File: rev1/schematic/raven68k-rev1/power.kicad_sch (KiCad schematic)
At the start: 36 parts, among them IC1 L5970D013TR, IC2 L5970D013TR, J3 Jack-DC, SW2 POWER_SW

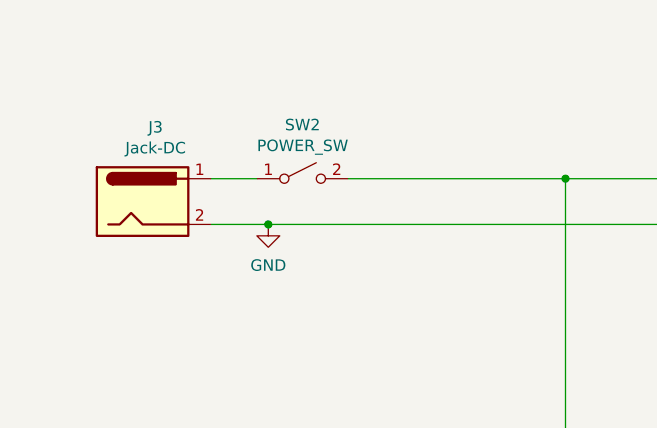
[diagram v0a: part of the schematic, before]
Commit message: board layout complete, needs verification
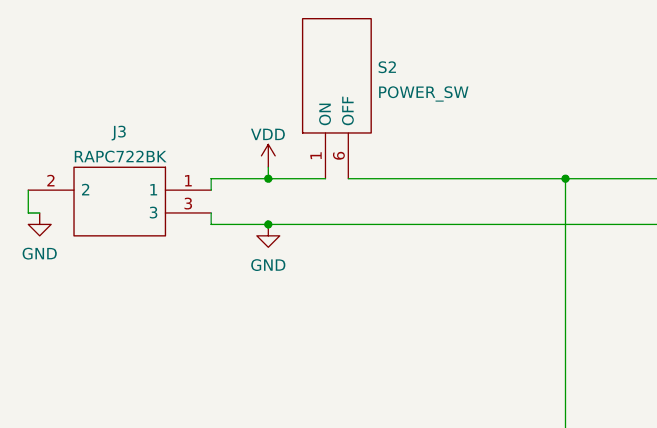
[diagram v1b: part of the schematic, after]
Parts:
- removed J3: Jack-DC, raven68k-rev1:RAPC722BK, symbol Connector:Jack-DC
- removed SW2: POWER_SW, raven68k-rev1:10TC605, symbol Switch:SW_SPST
- added J3: RAPC722BK, raven68k-rev1:RAPC722BK, symbol custom:RAPC722BK
- added S2: POWER_SW, raven68k-rev1:GPTS203212B, symbol custom:GPTS203212B
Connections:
- net GND: now also J3.2, J3.3
- net at C12.2, C13.2, C14.2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: now also S2.6 (OFF)
- new net VDD: J3.1, S2.1 (ON)
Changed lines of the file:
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@@
 (kicad_sch (version 20211123) (generator eeschema)
   (paper "A4")
+  (junction (at 73.66 57.15) (diameter 0) (color 0 0 0 0)
+  )
   (junction (at 231.14 53.34) (diameter 0) (color 0 0 0 0)
   )
@@
   (junction (at 254 149.86) (diameter 0) (color 0 0 0 0)
   )
+  (junction (at 40.64 57.15) (diameter 0) (color 0 0 0 0)
+  )
   (junction (at 231.14 115.57) (diameter 0) (color 0 0 0 0)
   )
@@
   )
   (junction (at 124.46 64.77) (diameter 0) (color 0 0 0 0)
-  )
-  (junction (at 73.66 57.15) (diameter 0) (color 0 0 0 0)
   )
   (junction (at 242.57 87.63) (diameter 0) (color 0 0 0 0)
@@
     (stroke (width 0) (type default) (color 0 0 0 0))
   )
+  (wire (pts (xy 34.29 57.15) (xy 34.29 58.42))
+    (stroke (width 0) (type default) (color 0 0 0 0))
+  )
   (wire (pts (xy 134.62 130.81) (xy 134.62 127))
     (stroke (width 0) (type default) (color 0 0 0 0))
@@
     (stroke (width 0) (type default) (color 0 0 0 0))
   )
+  (wire (pts (xy 40.64 57.15) (xy 46.99 57.15))
+    (stroke (width 0) (type default) (color 0 0 0 0))
+  )
   (wire (pts (xy 201.93 81.28) (xy 201.93 87.63))
     (stroke (width 0) (type default) (color 0 0 0 0))
@@
     (stroke (width 0) (type default) (color 0 0 0 0))
   )
+  (wire (pts (xy 40.64 55.88) (xy 40.64 57.15))
+    (stroke (width 0) (type default) (color 0 0 0 0))
+  )
   (wire (pts (xy 219.71 71.12) (xy 219.71 63.5))
     (stroke (width 0) (type default) (color 0 0 0 0))
@@
     (stroke (width 0) (type default) (color 0 0 0 0))
   )
+  (wire (pts (xy 13.97 58.42) (xy 13.97 60.96))
+    (stroke (width 0) (type default) (color 0 0 0 0))
+  )
   (wire (pts (xy 134.62 87.63) (xy 152.4 87.63))
     (stroke (width 0) (type default) (color 0 0 0 0))
@@
     (stroke (width 0) (type default) (color 0 0 0 0))
   )
+  (wire (pts (xy 49.53 57.15) (xy 73.66 57.15))
+    (stroke (width 0) (type default) (color 0 0 0 0))
+  )
   (wire (pts (xy 266.7 59.69) (xy 266.7 53.34))
     (stroke (width 0) (type default) (color 0 0 0 0))
@@
     (stroke (width 0) (type default) (color 0 0 0 0))
   )
+  (wire (pts (xy 34.29 60.96) (xy 34.29 62.23))
+    (stroke (width 0) (type default) (color 0 0 0 0))
+  )
   (wire (pts (xy 86.36 62.23) (xy 86.36 87.63))
     (stroke (width 0) (type default) (color 0 0 0 0))
   )
-  (wire (pts (xy 34.29 57.15) (xy 39.37 57.15))
-    (stroke (width 0) (type default) (color 0 0 0 0))
-  )
   (wire (pts (xy 73.66 57.15) (xy 104.14 57.15))
     (stroke (width 0) (type default) (color 0 0 0 0))
@@
     (stroke (width 0) (type default) (color 0 0 0 0))
   )
+  (wire (pts (xy 13.97 60.96) (xy 15.24 60.96))
+    (stroke (width 0) (type default) (color 0 0 0 0))
+  )
   (wire (pts (xy 190.5 125.73) (xy 190.5 133.35))
     (stroke (width 0) (type default) (color 0 0 0 0))
@@
     (stroke (width 0) (type default) (color 0 0 0 0))
   )
+  (wire (pts (xy 34.29 57.15) (xy 40.64 57.15))
+    (stroke (width 0) (type default) (color 0 0 0 0))
+  )
   (wire (pts (xy 242.57 129.54) (xy 242.57 115.57))
     (stroke (width 0) (type default) (color 0 0 0 0))
@@
   )
   (wire (pts (xy 173.99 115.57) (xy 177.8 115.57))
-    (stroke (width 0) (type default) (color 0 0 0 0))
-  )
-  (wire (pts (xy 49.53 57.15) (xy 73.66 57.15))
     (stroke (width 0) (type default) (color 0 0 0 0))
   )
@@
     (pin "2")
   )
-  (symbol (lib_id "Connector:Jack-DC") (at 26.67 59.69 0) (unit 1)
-    (in_bom yes) (on_board yes)
-    (property "Reference" "J3" (id 0) (at 28.1178 51.435 0))
-    (property "Value" "Jack-DC" (id 1) (at 28.1178 53.7464 0))
-    (property "Footprint" "raven68k-rev1:RAPC722BK" (id 2) (at 27.94 60.706 0)
-      (effects (font (size 1.27 1.27)) hide)
-    )
-    (property "Datasheet" "~" (id 3) (at 27.94 60.706 0)
-      (effects (font (size 1.27 1.27)) hide)
-    )
-    (pin "1")
-    (pin "2")
-  )
   (symbol (lib_id "power:+5V") (at 280.67 53.34 0) (unit 1)
     (in_bom yes) (on_board yes)
@@
     (pin "2")
   )
-  (symbol (lib_id "Switch:SW_SPST") (at 44.45 57.15 0) (unit 1)
-    (in_bom yes) (on_board yes)
-    (property "Reference" "SW2" (id 0) (at 44.45 51.181 0))
-    (property "Value" "POWER_SW" (id 1) (at 44.45 53.4924 0))
-    (property "Footprint" "raven68k-rev1:10TC605" (id 2) (at 44.45 57.15 0)
-      (effects (font (size 1.27 1.27)) hide)
-    )
-    (property "Datasheet" "~" (id 3) (at 44.45 57.15 0)
-      (effects (font (size 1.27 1.27)) hide)
-    )
-    (pin "1")
-    (pin "2")
+  (symbol (lib_id "custom:RAPC722BK") (at 34.29 58.42 0) (mirror y) (unit 1)
+    (in_bom yes) (on_board yes) (fields_autoplaced)
+    (property "Reference" "J3" (id 0) (at 24.13 51.9643 0))
+    (property "Value" "RAPC722BK" (id 1) (at 24.13 54.7394 0))
+    (property "Footprint" "raven68k-rev1:RAPC722BK" (id 2) (at 17.78 55.88 0)
+      (effects (font (size 1.27 1.27)) (justify left) hide)
+    )
+    (property "Datasheet" "http://www.mouser.com/datasheet/2/393/rapc722x_cd-371352.pdf" (id 3) (at 17.78 58.42 0)
+      (effects (font (size 1.27 1.27)) (justify left) hide)
+    )
+    (property "Description" "SWITCHCRAFT/CONXALL - RAPC722BK - CONNECTOR, DC POWER, SOCKET, 5A, THT" (id 4) (at 17.78 60.96 0)
+      (effects (font (size 1.27 1.27)) (justify left) hide)
+    )
+    (property "Height" "11" (id 5) (at 17.78 63.5 0)
+      (effects (font (size 1.27 1.27)) (justify left) hide)
+    )
+    (property "Manufacturer_Name" "Switchcraft" (id 6) (at 17.78 66.04 0)
+      (effects (font (size 1.27 1.27)) (justify left) hide)
+    )
+    (property "Manufacturer_Part_Number" "RAPC722BK" (id 7) (at 17.78 68.58 0)
+      (effects (font (size 1.27 1.27)) (justify left) hide)
+    )
+    (property "Mouser Part Number" "502-RAPC722BK" (id 8) (at 17.78 71.12 0)
+      (effects (font (size 1.27 1.27)) (justify left) hide)
+    )
+    (property "Mouser Price/Stock" "https://www.mouser.co.uk/ProductDetail/Switchcraft/RAPC722BK?qs=Nl9mtr8tY%2Fsf3BOYJcSXfg%3D%3D" (id 9) (at 17.78 73.66 0)
+      (effects (font (size 1.27 1.27)) (justify left) hide)
+    )
+    (property "Arrow Part Number" "RAPC722BK" (id 10) (at 17.78 76.2 0)
+      (effects (font (size 1.27 1.27)) (justify left) hide)
+    )
+    (property "Arrow Price/Stock" "https://www.arrow.com/en/products/rapc722bk/switchcraft" (id 11) (at 17.78 78.74 0)
+      (effects (font (size 1.27 1.27)) (justify left) hide)
+    )
+    (pin "1")
+    (pin "2")
+    (pin "3")
   )
   (symbol (lib_id "power:GND") (at 40.64 62.23 0) (unit 1)
@@
     (pin "1")
   )
+  (symbol (lib_id "power:VDD") (at 40.64 55.88 0) (unit 1)
+    (in_bom yes) (on_board yes) (fields_autoplaced)
+    (property "Reference" "#PWR0105" (id 0) (at 40.64 59.69 0)
+      (effects (font (size 1.27 1.27)) hide)
+    )
+    (property "Value" "VDD" (id 1) (at 40.64 52.2755 0))
+    (property "Footprint" "" (id 2) (at 40.64 55.88 0)
+      (effects (font (size 1.27 1.27)) hide)
+    )
+    (property "Datasheet" "" (id 3) (at 40.64 55.88 0)
+      (effects (font (size 1.27 1.27)) hide)
+    )
+    (pin "1")
+  )
+  (symbol (lib_id "power:GND") (at 15.24 60.96 0) (unit 1)
+    (in_bom yes) (on_board yes) (fields_autoplaced)
+    (property "Reference" "#PWR?" (id 0) (at 15.24 67.31 0)
+      (effects (font (size 1.27 1.27)) hide)
+    )
+    (property "Value" "GND" (id 1) (at 15.24 65.5225 0))
+    (property "Footprint" "" (id 2) (at 15.24 60.96 0)
+      (effects (font (size 1.27 1.27)) hide)
+    )
+    (property "Datasheet" "" (id 3) (at 15.24 60.96 0)
+      (effects (font (size 1.27 1.27)) hide)
+    )
+    (pin "1")
+  )
+  (symbol (lib_id "custom:GPTS203212B") (at 46.99 57.15 90) (unit 1)
+    (in_bom yes) (on_board yes) (fields_autoplaced)
+    (property "Reference" "S2" (id 0) (at 52.7812 44.8115 90)
+      (effects (font (size 1.27 1.27)) (justify right))
+    )
+    (property "Value" "POWER_SW" (id 1) (at 52.7812 47.5866 90)
+      (effects (font (size 1.27 1.27)) (justify right))
+    )
+    (property "Footprint" "raven68k-rev1:GPTS203212B" (id 2) (at 44.45 38.1 0)
+      (effects (font (size 1.27 1.27)) (justify left) hide)
+    )
+    (property "Datasheet" "http://switches-connectors-custom.cwind.com/Asset/GPTS203212BR2.pdf" (id 3) (at 46.99 38.1 0)
+      (effects (font (size 1.27 1.27)) (justify left) hide)
+    )
+    (property "Description" "Pushbutton Switches SPST ON-OFF" (id 4) (at 49.53 38.1 0)
+      (effects (font (size 1.27 1.27)) (justify left) hide)
+    )
+    (property "Height" "12" (id 5) (at 52.07 38.1 0)
+      (effects (font (size 1.27 1.27)) (justify left) hide)
+    )
+    (property "Manufacturer_Name" "CW Industries" (id 6) (at 54.61 38.1 0)
+      (effects (font (size 1.27 1.27)) (justify left) hide)
+    )
+    (property "Manufacturer_Part_Number" "GPTS203212B" (id 7) (at 57.15 38.1 0)
+      (effects (font (size 1.27 1.27)) (justify left) hide)
+    )
+    (property "Mouser Part Number" "629-GPTS203212B" (id 8) (at 59.69 38.1 0)
+      (effects (font (size 1.27 1.27)) (justify left) hide)
+    )
+    (property "Mouser Price/Stock" "https://www.mouser.com/Search/Refine.aspx?Keyword=629-GPTS203212B" (id 9) (at 62.23 38.1 0)
+      (effects (font (size 1.27 1.27)) (justify left) hide)
+    )
+    (property "Arrow Part Number" "" (id 10) (at 64.77 38.1 0)
+      (effects (font (size 1.27 1.27)) (justify left) hide)
+    )
+    (property "Arrow Price/Stock" "" (id 11) (at 67.31 38.1 0)
+      (effects (font (size 1.27 1.27)) (justify left) hide)
+    )
+    (pin "1")
+    (pin "6")
+  )
 )

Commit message: some helpful labels
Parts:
- C12, C13: LCSC (none) -> C24497
- C14, C15: LCSC (none) -> C13585
- C16, C17: LCSC (none) -> C1854
- C18, C19: LCSC (none) -> C97929
- C20, C21: LCSC (none) -> C1868
- C26, C27: value 100nF -> 0.1uF; LCSC (none) -> C24497
- R11, R12: LCSC (none) -> C17936
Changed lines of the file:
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@@
+      (effects (font (size 1.27 1.27)) hide)
+    )
+    (property "LCSC" "C1868" (id 4) (at 210.82 71.12 90)
       (effects (font (size 1.27 1.27)) hide)
     )
@@
       (effects (font (size 1.27 1.27)) (justify right))
     )
-    (property "Value" "100nF" (id 1) (at 256.3368 70.993 0)
+    (property "Value" "0.1uF" (id 1) (at 256.3368 70.993 0)
       (effects (font (size 1.27 1.27)) (justify right))
     )
@@
       (effects (font (size 1.27 1.27)) hide)
     )
+    (property "LCSC" "C24497" (id 4) (at 254 69.85 0)
+      (effects (font (size 1.27 1.27)) hide)
+    )
     (pin "1")
     (pin "2")
@@
       (effects (font (size 1.27 1.27)) hide)
     )
+    (property "LCSC" "C24497" (id 4) (at 104.14 71.12 0)
+      (effects (font (size 1.27 1.27)) hide)
+    )
     (pin "1")
     (pin "2")
@@
       (effects (font (size 1.27 1.27)) hide)
     )
+    (property "LCSC" "C13585" (id 4) (at 114.3 71.12 0)
+      (effects (font (size 1.27 1.27)) hide)
+    )
     (pin "1")
     (pin "2")
@@
       (effects (font (size 1.27 1.27)) hide)
     )
+    (property "LCSC" "C1854" (id 4) (at 124.46 71.12 0)
+      (effects (font (size 1.27 1.27)) hide)
+    )
     (pin "1")
     (pin "2")
@@
       (effects (font (size 1.27 1.27)) hide)
     )
+    (property "LCSC" "C97929" (id 4) (at 134.62 71.12 0)
+      (effects (font (size 1.27 1.27)) hide)
+    )
     (pin "1")
     (pin "2")
@@
     )
     (property "Datasheet" "~" (id 3) (at 134.62 81.28 0)
+      (effects (font (size 1.27 1.27)) hide)
+    )
+    (property "LCSC" "C17936" (id 4) (at 134.62 81.28 0)
       (effects (font (size 1.27 1.27)) hide)
     )
@@
       (effects (font (size 1.27 1.27)) hide)
     )
+    (property "LCSC" "C1868" (id 4) (at 210.82 133.35 90)
+      (effects (font (size 1.27 1.27)) hide)
+    )
     (pin "1")
     (pin "2")
@@
       (effects (font (size 1.27 1.27)) (justify right))
     )
-    (property "Value" "100nF" (id 1) (at 256.3368 133.223 0)
+    (property "Value" "0.1uF" (id 1) (at 256.3368 133.223 0)
       (effects (font (size 1.27 1.27)) (justify right))
     )
@@
       (effects (font (size 1.27 1.27)) hide)
     )
+    (property "LCSC" "C24497" (id 4) (at 254 132.08 0)
+      (effects (font (size 1.27 1.27)) hide)
+    )
     (pin "1")
     (pin "2")
@@
       (effects (font (size 1.27 1.27)) hide)
     )
+    (property "LCSC" "C24497" (id 4) (at 104.14 133.35 0)
+      (effects (font (size 1.27 1.27)) hide)
+    )
     (pin "1")
     (pin "2")
@@
       (effects (font (size 1.27 1.27)) hide)
     )
+    (property "LCSC" "C13585" (id 4) (at 114.3 133.35 0)
+      (effects (font (size 1.27 1.27)) hide)
+    )
     (pin "1")
     (pin "2")
@@
       (effects (font (size 1.27 1.27)) hide)
     )
+    (property "LCSC" "C1854" (id 4) (at 124.46 133.35 0)
+      (effects (font (size 1.27 1.27)) hide)
+    )
     (pin "1")
     (pin "2")
@@
       (effects (font (size 1.27 1.27)) hide)
     )
+    (property "LCSC" "C97929" (id 4) (at 134.62 133.35 0)
+      (effects (font (size 1.27 1.27)) hide)
+    )
     (pin "1")
     (pin "2")
@@
       (effects (font (size 1.27 1.27)) hide)
     )
+    (property "LCSC" "C17936" (id 4) (at 134.62 143.51 0)
+      (effects (font (size 1.27 1.27)) hide)
+    )
